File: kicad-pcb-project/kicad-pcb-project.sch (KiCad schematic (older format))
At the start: 150 parts

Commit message: adding type-c submodules to project
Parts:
- added USB?: HRO-TYPE-C-31-M-12, symbol Type-C:HRO-TYPE-C-31-M-12
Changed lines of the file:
@@
 Wire Wire Line
 	3600 3130 3600 3230
+$Comp
+L Type-C:HRO-TYPE-C-31-M-12 USB?
+U 1 1 5F8EF13C
+P 6000 2310
+F 0 "USB?" H 5833 3107 60  0000 C CNN
+F 1 "HRO-TYPE-C-31-M-12" H 5833 3001 60  0000 C CNN
+F 2 "" H 6000 2310 60  0001 C CNN
+F 3 "" H 6000 2310 60  0001 C CNN
+	1    6000 2310
+	1    0    0    -1
+$EndComp
 $EndSCHEMATC

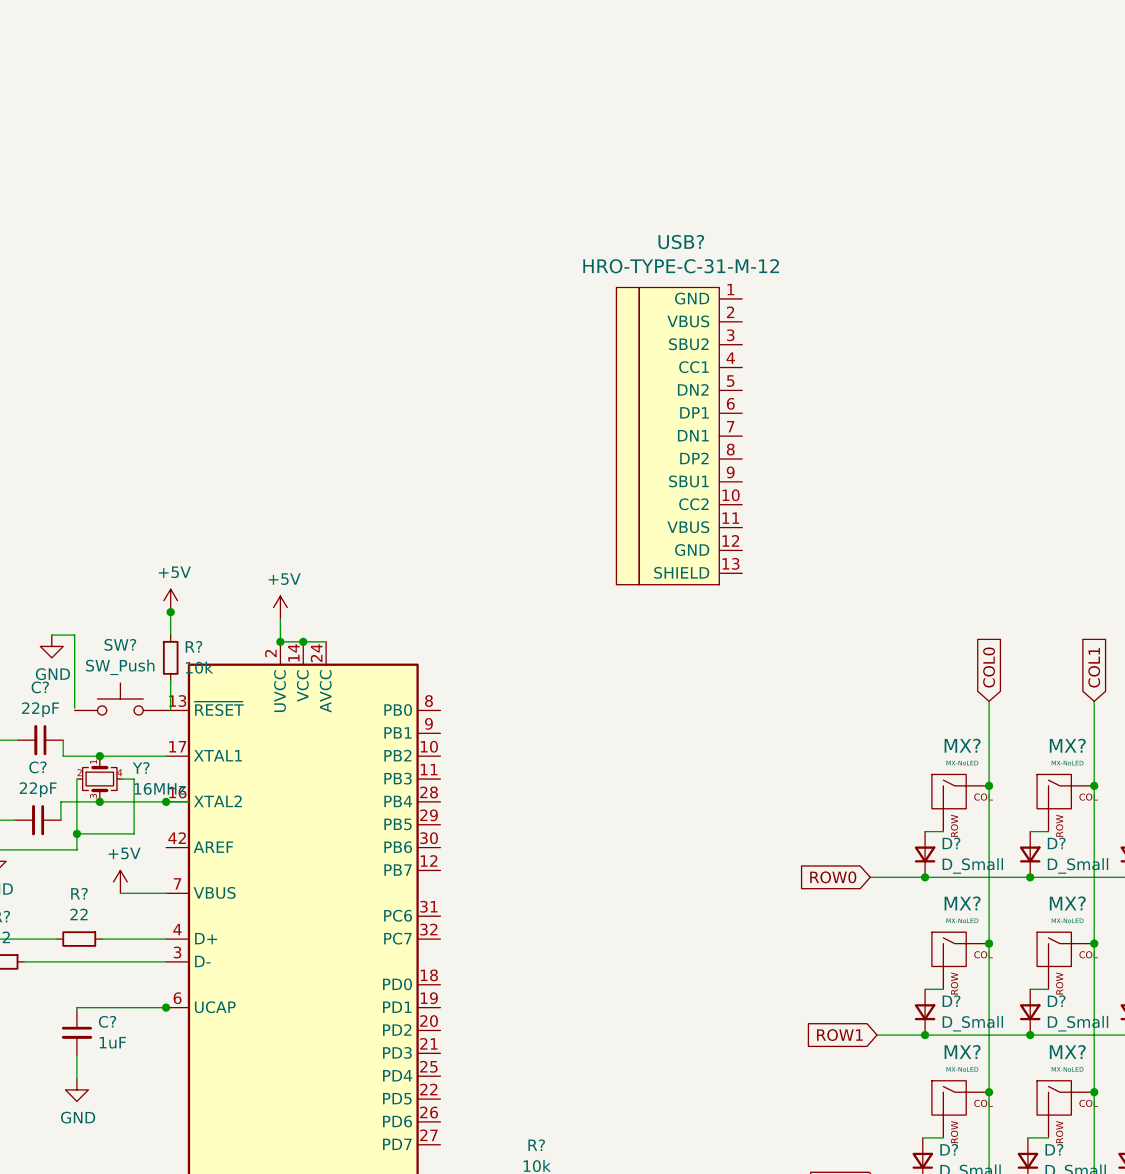
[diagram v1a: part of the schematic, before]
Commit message: added usb-c to schematic
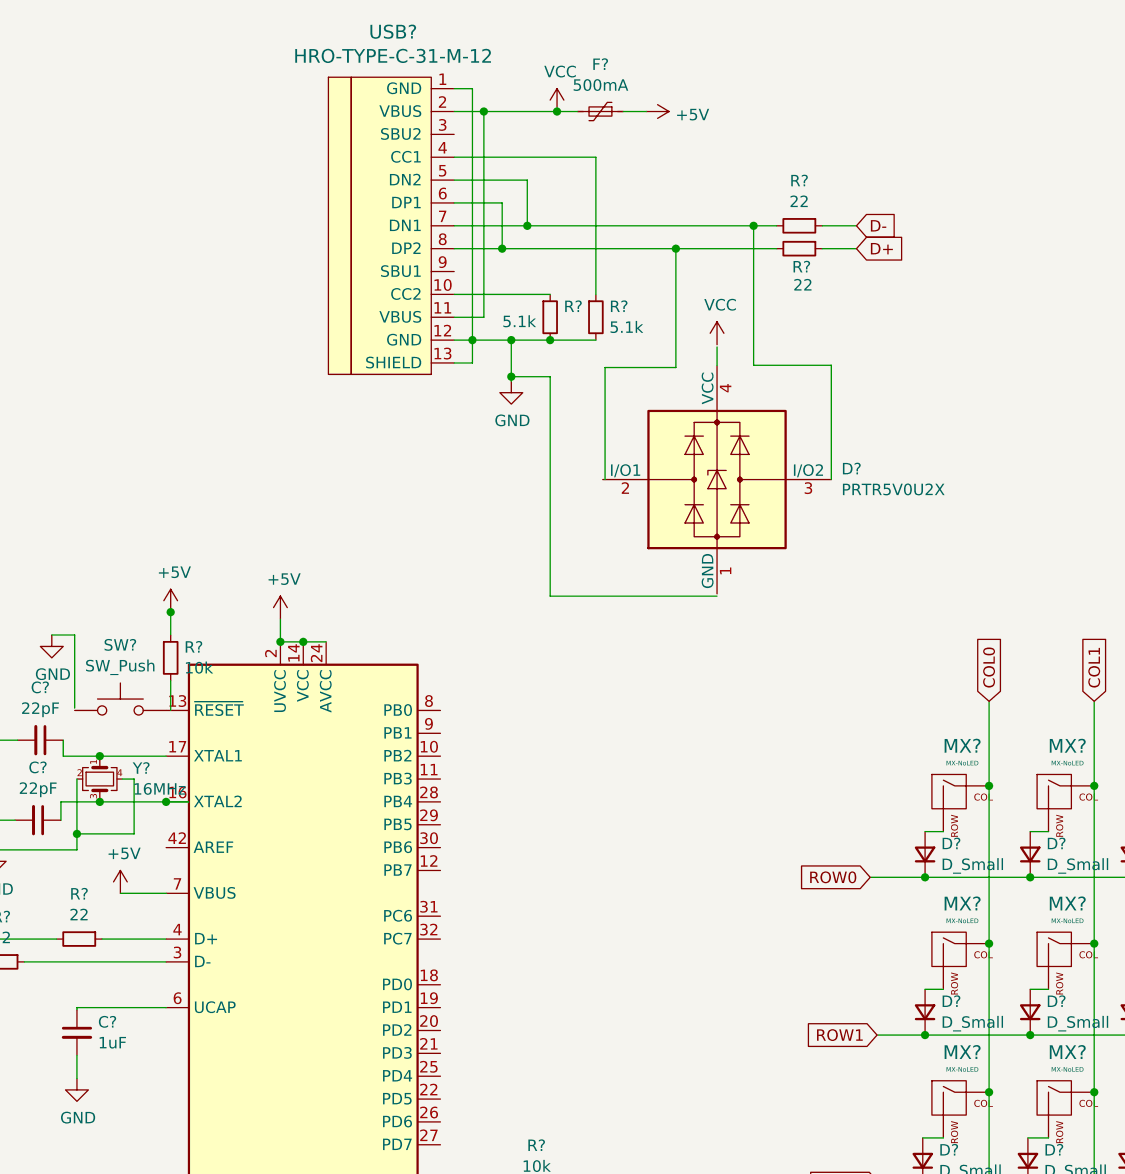
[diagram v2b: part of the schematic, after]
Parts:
- added D?: PRTR5V0U2X, Package_TO_SOT_SMD:SOT-143, symbol Power_Protection:PRTR5V0U2X
- added F?: 500mA, symbol Device:Polyfuse_Small
- added R? (x2): 22, symbol Device:R_Small
- added R? (x2): 5.1k, symbol Device:R_Small
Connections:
- net +5V: now also F?.1
- net D+: now also R?.1
- net D-: now also R?.1
- net GND: now also USB?.1 (GND), USB?.12 (GND), USB?.13 (SHIELD), R?.2, R?.2
- net at USB?.10 (CC2): now also R?.1
- net VCC: now reaches USB?.11 (VBUS)
- net VCC: now also USB?.2 (VBUS), F?.2
- net at USB?.4 (CC1): now also R?.1
- net at USB?.5 (DN2): now also USB?.7 (DN1), D?.3 (I/O2), R?.2
- net at USB?.6 (DP1): now also USB?.8 (DP2), R?.2
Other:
- moved on the sheet: USB?
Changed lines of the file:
@@
 $EndComp
-Wire Wire Line
-	3590 4860 3580 4860
 Wire Wire Line
 	3190 4860 3190 4870
 Wire Wire Line
 	3190 5070 3190 5170
-Connection ~ 3580 4860
-Wire Wire Line
-	3580 4860 3190 4860
 $Comp
 L Device:C_Small C?
@@
 L Type-C:HRO-TYPE-C-31-M-12 USB?
 U 1 1 5F8EF13C
-P 6000 2310
-F 0 "USB?" H 5833 3107 60  0000 C CNN
-F 1 "HRO-TYPE-C-31-M-12" H 5833 3001 60  0000 C CNN
-F 2 "" H 6000 2310 60  0001 C CNN
-F 3 "" H 6000 2310 60  0001 C CNN
-	1    6000 2310
-	1    0    0    -1
-$EndComp
+P 4740 1390
+F 0 "USB?" H 4573 2187 60  0000 C CNN
+F 1 "HRO-TYPE-C-31-M-12" H 4573 2081 60  0000 C CNN
+F 2 "" H 4740 1390 60  0001 C CNN
+F 3 "" H 4740 1390 60  0001 C CNN
+	1    4740 1390
+	1    0    0    -1
+$EndComp
+$Comp
+L Device:R_Small R?
+U 1 1 5F9027B8
+P 6350 1540
+F 0 "R?" V 6460 1550 50  0000 C BNN
+F 1 "22" V 6510 1600 50  0000 R CNN
+F 2 "" H 6350 1540 50  0001 C CNN
+F 3 "~" H 6350 1540 50  0001 C CNN
+	1    6350 1540
+	0    1    1    0
+$EndComp
+Text GLabel 6600 1540 2    50   Input ~ 0
+D+
+Wire Wire Line
+	6600 1540 6450 1540
+Wire Wire Line
+	4840 1340 5050 1340
+$Comp
+L Device:R_Small R?
+U 1 1 5F96A43A
+P 6350 1440
+F 0 "R?" V 6154 1440 50  0000 C CNN
+F 1 "22" V 6245 1440 50  0000 C CNN
+F 2 "" H 6350 1440 50  0001 C CNN
+F 3 "~" H 6350 1440 50  0001 C CNN
+	1    6350 1440
+	0    1    1    0
+$EndComp
+Text GLabel 6600 1440 2    50   Input ~ 0
+D-
+Wire Wire Line
+	6600 1440 6450 1440
+Wire Wire Line
+	4840 1440 5160 1440
+Wire Wire Line
+	4840 1240 5160 1240
+Wire Wire Line
+	5160 1240 5160 1440
+Wire Wire Line
+	4840 2040 4920 2040
+Wire Wire Line
+	4840 840  4920 840
+Wire Wire Line
+	4840 1940 4920 1940
+Connection ~ 4920 1940
+Wire Wire Line
+	4920 1940 4920 2040
+Wire Wire Line
+	4840 1840 4970 1840
+Wire Wire Line
+	4970 940  4970 1840
+Wire Wire Line
+	4970 940  4840 940
+Wire Wire Line
+	3580 4860 3190 4860
+Wire Wire Line
+	4970 940  5290 940
+Connection ~ 4970 940
+$Comp
+L power:+5V #PWR?
+U 1 1 5FD2A6CB
+P 5680 940
+F 0 "#PWR?" H 5680 790 50  0001 C CNN
+F 1 "+5V" V 5695 1068 50  0000 L CNN
+F 2 "" H 5680 940 50  0001 C CNN
+F 3 "" H 5680 940 50  0001 C CNN
+	1    5680 940
+	0    1    1    0
+$EndComp
+$Comp
+L Device:Polyfuse_Small F?
+U 1 1 5FD2C00E
+P 5480 940
+F 0 "F?" V 5275 940 50  0000 C CNN
+F 1 "500mA" V 5366 940 50  0000 C CNN
+F 2 "" H 5530 740 50  0001 L CNN
+F 3 "~" H 5480 940 50  0001 C CNN
+	1    5480 940
+	0    1    1    0
+$EndComp
+Wire Wire Line
+	5680 940  5580 940
+$Comp
+L Device:R_Small R?
+U 1 1 5FD46B9D
+P 5460 1840
+F 0 "R?" H 5519 1886 50  0000 L CNN
+F 1 "5.1k" H 5519 1795 50  0000 L CNN
+F 2 "" H 5460 1840 50  0001 C CNN
+F 3 "~" H 5460 1840 50  0001 C CNN
+	1    5460 1840
+	1    0    0    -1
+$EndComp
+$Comp
+L Device:R_Small R?
+U 1 1 5FD48619
+P 5260 1840
+F 0 "R?" H 5319 1886 50  0000 L CNN
+F 1 "5.1k" H 5050 1820 50  0000 L CNN
+F 2 "" H 5260 1840 50  0001 C CNN
+F 3 "~" H 5260 1840 50  0001 C CNN
+	1    5260 1840
+	1    0    0    -1
+$EndComp
+Wire Wire Line
+	5050 1340 5050 1540
+Wire Wire Line
+	4840 1540 5050 1540
+Connection ~ 5050 1540
+Connection ~ 5160 1440
+Wire Wire Line
+	5050 1540 5810 1540
+Wire Wire Line
+	5160 1440 6150 1440
+Wire Wire Line
+	4920 840  4920 1940
+Wire Wire Line
+	4920 1940 5090 1940
+Connection ~ 5260 1940
+Wire Wire Line
+	5260 1940 5460 1940
+Wire Wire Line
+	4840 1740 5260 1740
+Wire Wire Line
+	4840 1140 5460 1140
+Wire Wire Line
+	5460 1140 5460 1740
+$Comp
+L power:GND #PWR?
+U 1 1 5FEC8911
+P 5090 2120
+F 0 "#PWR?" H 5090 1870 50  0001 C CNN
+F 1 "GND" H 5095 1947 50  0000 C CNN
+F 2 "" H 5090 2120 50  0001 C CNN
+F 3 "" H 5090 2120 50  0001 C CNN
+	1    5090 2120
+	1    0    0    -1
+$EndComp
+Connection ~ 5090 1940
+Wire Wire Line
+	5090 1940 5260 1940
+$Comp
+L power:VCC #PWR?
+U 1 1 5FFBF056
+P 5290 940
+F 0 "#PWR?" H 5290 790 50  0001 C CNN
+F 1 "VCC" H 5305 1113 50  0000 C CNN
+F 2 "" H 5290 940 50  0001 C CNN
+F 3 "" H 5290 940 50  0001 C CNN
+	1    5290 940
+	1    0    0    -1
+$EndComp
+Wire Wire Line
+	5290 940  5380 940
+Connection ~ 5290 940
+$Comp
+L Power_Protection:PRTR5V0U2X D?
+U 1 1 5FFEE231
+P 5990 2550
+F 0 "D?" H 6534 2596 50  0000 L CNN
+F 1 "PRTR5V0U2X" H 6534 2505 50  0000 L CNN
+F 2 "Package_TO_SOT_SMD:SOT-143" H 6050 2550 50  0001 C CNN
+F 3 "https://assets.nexperia.com/documents/data-sheet/PRTR5V0U2X.pdf" H 6050 2550 50  0001 C CNN
+	1    5990 2550
+	1    0    0    -1
+$EndComp
+Wire Wire Line
+	5090 1940 5090 2100
+Wire Wire Line
+	5990 3060 5260 3060
+Wire Wire Line
+	5260 3060 5260 2100
+Wire Wire Line
+	5260 2100 5090 2100
+Connection ~ 5090 2100
+Wire Wire Line
+	5090 2100 5090 2120
+$Comp
+L power:VCC #PWR?
+U 1 1 60107DA4
+P 5990 1960
+F 0 "#PWR?" H 5990 1810 50  0001 C CNN
+F 1 "VCC" H 6005 2133 50  0000 C CNN
+F 2 "" H 5990 1960 50  0001 C CNN
+F 3 "" H 5990 1960 50  0001 C CNN
+	1    5990 1960
+	1    0    0    -1
+$EndComp
+Wire Wire Line
+	5990 1970 5990 2050
+Wire Wire Line
+	5500 2550 5500 2060
+Wire Wire Line
+	5500 2060 5810 2060
+Wire Wire Line
+	5810 2060 5810 1540
+Connection ~ 5810 1540
+Wire Wire Line
+	5810 1540 6250 1540
+Wire Wire Line
+	6490 2550 6490 2050
+Wire Wire Line
+	6490 2050 6150 2050
+Wire Wire Line
+	6150 2050 6150 1440
+Connection ~ 6150 1440
+Wire Wire Line
+	6150 1440 6250 1440
 $EndSCHEMATC

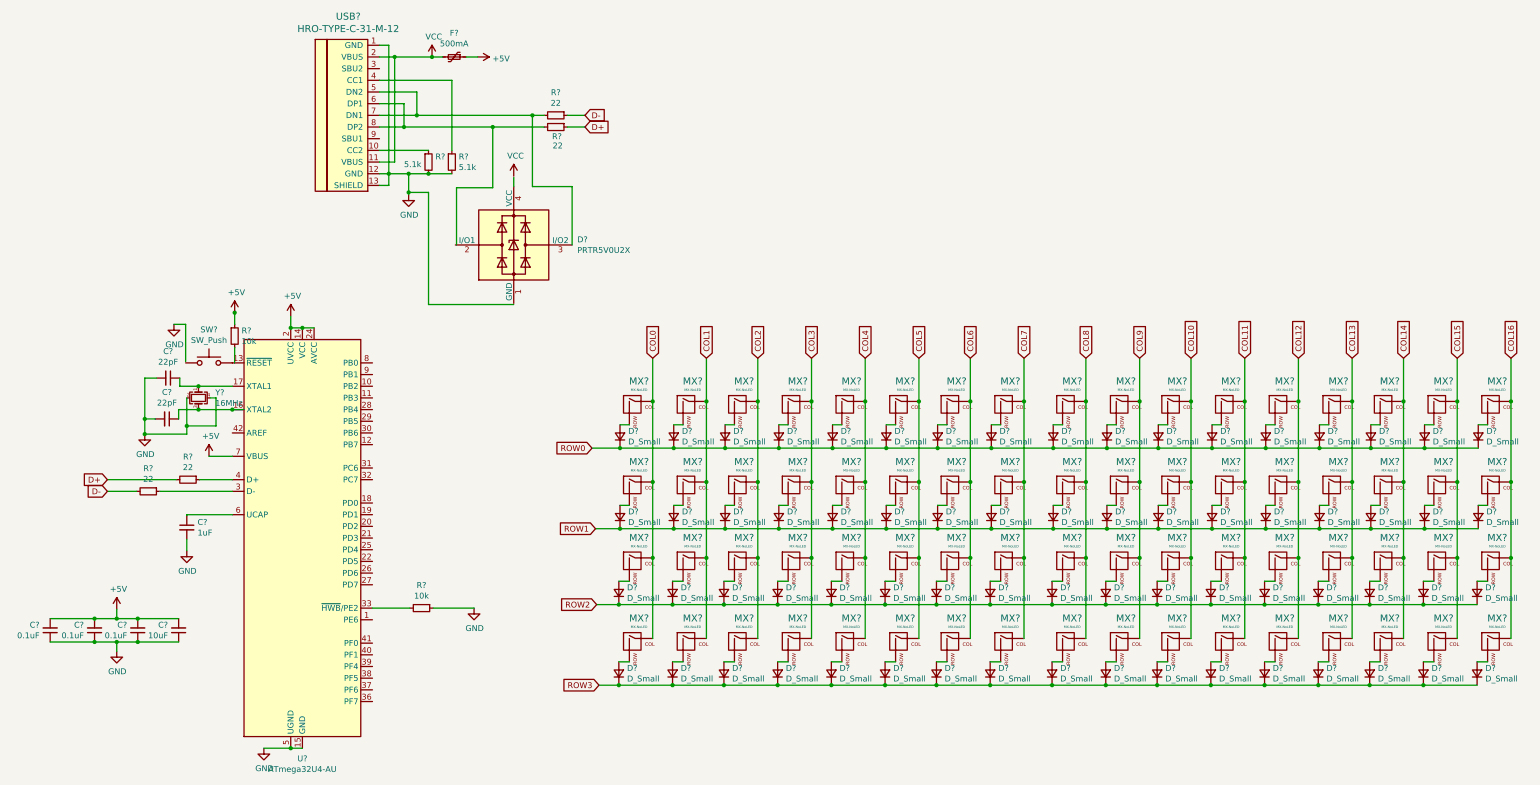
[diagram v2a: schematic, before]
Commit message: added footprints
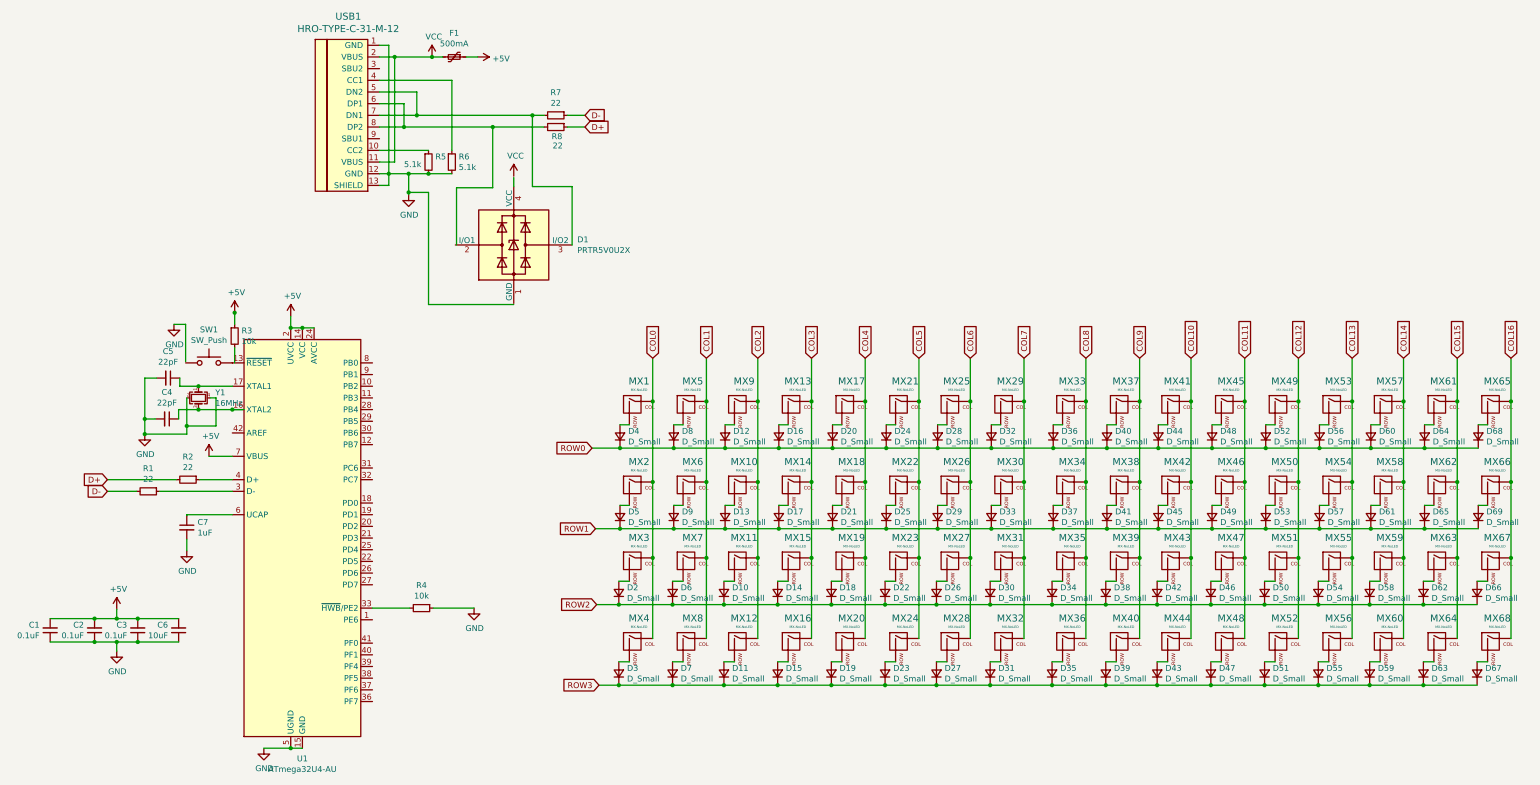
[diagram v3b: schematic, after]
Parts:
- C1, C2, C3, C4, C5, C6: renamed from C?; footprint (none) -> Capacitor_SMD:C_0805_2012Metric
- C7: renamed from C?; footprint (none) -> Diode_SMD:D_SOD-123
- D1: renamed from D?; footprint Package_TO_SOT_SMD:SOT-143 -> Diode_SMD:D_SOD-123
- D10, D11, D12, D13, D14, D15, D16, D17, D18, D19, D2, D20, D21, D22, D23, D24, D25, D26, D27, D28, D29, D3, D30, D31, D32, D33, D34, D35, D36, D37, D38, D39, D4, D40, D41, D42, D43, D44, D45, D46, D47, D48, D49, D5, D50, D51, D52, D53, D54, D55, D56, D57, D58, D59, D6, D60, D61, D62, D63, D64, D65, D66, D67, D68, D69, D7, D8, D9: renamed from D?; footprint (none) -> Diode_SMD:D_SOD-123
- F1: renamed from F?; footprint (none) -> Fuse:Fuse_1206_3216Metric
- MX1, MX10, MX11, MX12, MX13, MX14, MX15, MX16, MX17, MX18, MX19, MX2, MX20, MX21, MX22, MX23, MX24, MX25, MX26, MX27, MX28, MX29, MX3, MX30, MX31, MX32, MX33, MX34, MX35, MX36, MX37, MX38, MX39, MX4, MX40, MX41, MX42, MX43, MX44, MX45, MX46, MX47, MX48, MX49, MX5, MX50, MX51, MX52, MX53, MX54, MX55, MX56, MX57, MX58, MX59, MX6, MX60, MX61, MX62, MX63, MX64, MX65, MX66, MX67, MX68, MX7, MX8, MX9: renamed from MX?; footprint (none) -> keyswitches:Kailh_socket_MX
- R1, R2, R3, R4, R5, R6, R7, R8: renamed from R?; footprint (none) -> Resistor_SMD:R_0805_2012Metric
- SW1: renamed from SW?; footprint (none) -> random-keyboard-parts:SKQG-1155865
- USB1: renamed from USB?; footprint (none) -> Type-C:HRO-TYPE-C-31-M-12-Assembly
- Y1: renamed from Y?; footprint (none) -> Crystal:Crystal_SMD_3225-4Pin_3.2x2.5mm
- gave numbers to parts that had none: 1
